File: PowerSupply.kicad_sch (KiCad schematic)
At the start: 1 part, among them J201 Power

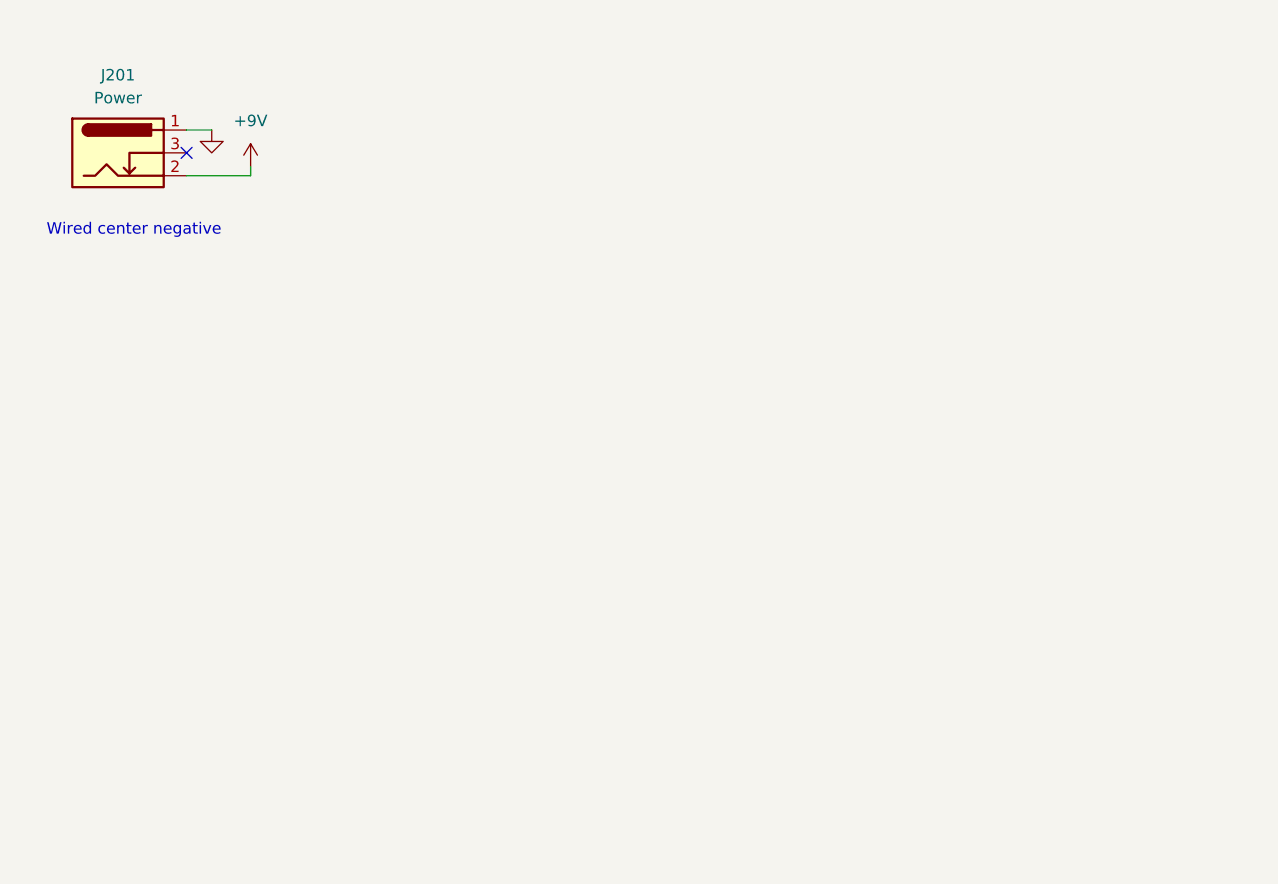
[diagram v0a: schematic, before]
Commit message: spice sim, start of schematic
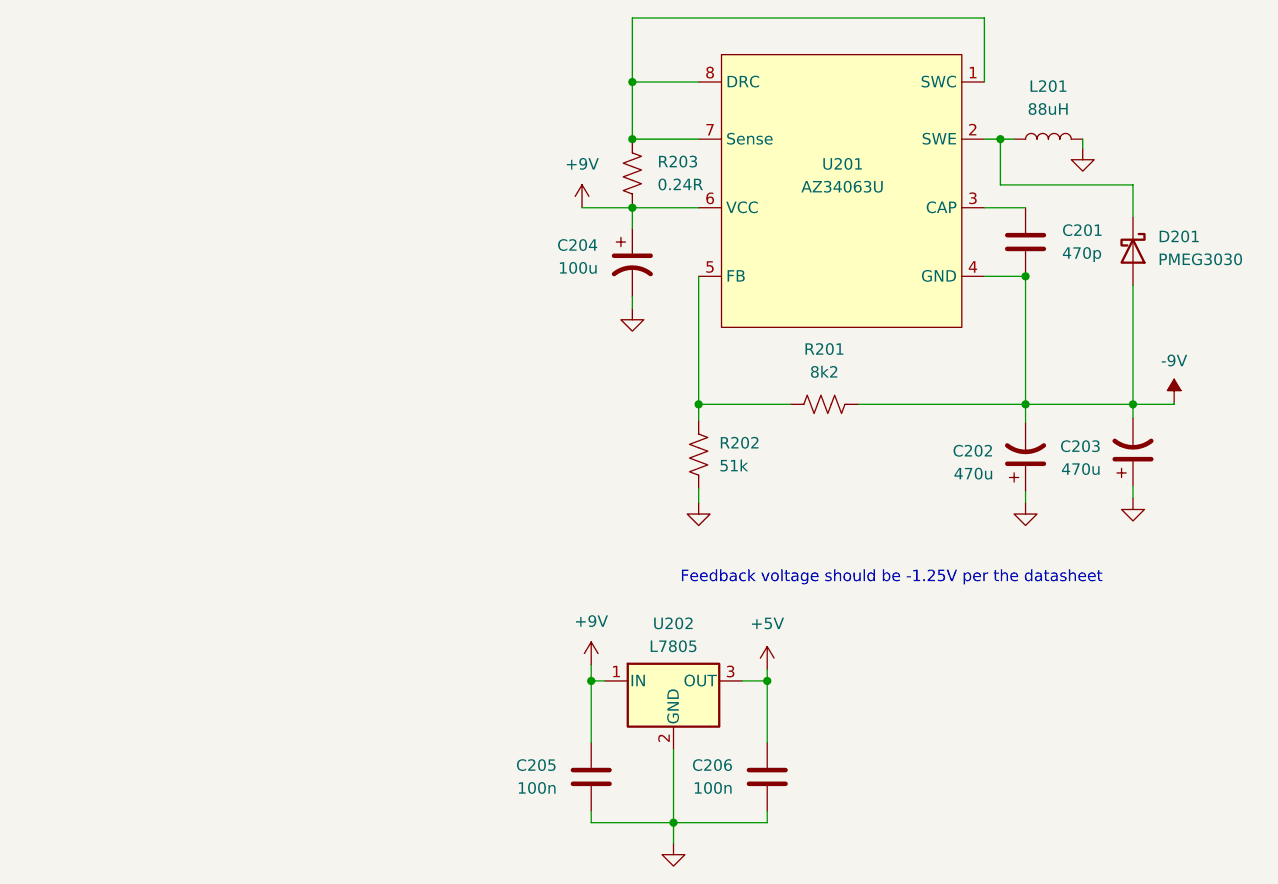
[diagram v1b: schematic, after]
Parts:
- removed J201: Power, Connector_BarrelJack:BarrelJack_Kycon_KLDX-0202-xC_Horizontal, symbol Connector:Barrel_Jack_Switch
- added C201: 470p, symbol Device:C
- added C202, C203: 470u, symbol Device:C_Polarized_US
- added C204: 100u, symbol Device:C_Polarized_US
- added C205, C206: 100n, symbol Device:C
- added D201: PMEG3030, Diode_SMD:D_SOD-123, symbol Device:D_Schottky
- added L201: 88uH, symbol Device:L
- added R201: 8k2, symbol Device:R_US
- added R202: 51k, symbol Device:R_US
- added R203: 0.24R, symbol Device:R_US
- added U201: AZ34063U, symbol Regulator_Switching:AZ34063U
- added U202: L7805, symbol Regulator_Linear:L7805
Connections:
- net +9V: now also C204.1, C205.1, R203.1, U201.6 (VCC), U202.1 (IN)
- net GND: now also C202.1, C203.1, C204.2, C205.2, C206.2, L201.2, R202.1, U202.2 (GND)
- new net: R203.2, U201.1 (SWC), U201.7 (Sense), U201.8 (DRC)
- new net: D201.1 (K), L201.1, U201.2 (SWE)
- new net: C201.1, U201.3 (CAP)
- new net: R201.1, R202.2, U201.5 (FB)
- new net +5V: C206.1, U202.3 (OUT)
- new net -9V: C201.2, C202.2, C203.2, D201.2 (A), R201.2, U201.4 (GND)
- no-connect marks 1 -> 0
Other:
- note added: "Feedback voltage should be -1.25V per the datasheet"
- note removed: "Wired center negative"
